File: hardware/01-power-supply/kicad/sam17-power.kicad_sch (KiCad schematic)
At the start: 31 parts, among them J1 12VAC CT 2A, J2 BUS +12/G/G/-12, J3 AC 230V IN, J4 TR1 pri (ext), U1 LM7812, U2 LM7912, U3 LM7805

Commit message: Add protective earth to module 1 and make the BOM verifiable
Closes the two documented gaps in the power-supply module, plus several
defects found while closing them.

Protective earth (design-notes.md section 13). J3 becomes a 3-position
block (L/N/PE); pin 3 drives an Earth_Protective symbol and stops there.
J5 is a new faston that carries circuit 0 V to the same chassis stud. PE
and GND stay separate nets on purpose - they meet in metal, off the
board, so fault current never runs through PCB copper.

The bond is hard rather than a ground-lift network because the panels are
galvanized sheet and the ~40 metal-bushing jacks already tie chassis to
GND at 40 points; a lift network would be shorted 40 times over. That
premise is stated explicitly, since isolated jacks would invalidate it.

J1 is a 3-position block, not 2: the transformer secondary is
centre-tapped and carries three conductors. The schematic was right and
bom.csv was stale.

Defects found while doing the above:

- J3/J4 were wired 0.36 mm off their real pins and only passed ERC
  because KiCad snaps within ~1 mm. The docstring note that "explained"
  those odd offsets was wrong; Conn_01x0N_Pin geometry is on-grid.
  build_schematic.py now aborts unless every pin has an exact wire
  vertex. This also removes the 3 off-grid warnings we had been carrying:
  ERC is now 0 errors, 0 warnings.
- The neutral ran straight through RV1's body. The varistor is 7.62 mm
  tall and J3's pins sit 2.54 apart, so it never fit; neutral now runs on
  its own lane.
- R3 is 680R, not the 2.2k the BOM listed for all three LEDs - at 5 V,
  2.2k gives ~1.3 mA and that indicator is invisible.
- bom.csv could not be cross-checked at all: it called RV1/NT1 MOV1/NTC1,
  and its C3/C4/C5 were different parts from the schematic's. It now
  carries a refs column, and check_bom.py verifies both directions.

Known gap, deliberately not fixed: the +5 V rail never leaves the board.
J2 is drawn with 4 pins (+12/GND/GND/-12) and the netlist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
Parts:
- removed J3: AC 230V IN, symbol Connector:Conn_01x02_Pin
- added J3: AC 230V IN, symbol Connector:Conn_01x03_Pin
- added J5: CHASIS, symbol Connector:Conn_01x01_Pin
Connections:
- net GND: now also J5.1 (Pin_1)
- net SEC_A: now reaches BR1.3, J1.1 (Pin_1)
- net SEC_B: now reaches BR1.4, J1.3 (Pin_3)
- net L: now reaches F1.1
- net L: now also J3.1 (Pin_1)
- net L_TR: now reaches J4.2 (Pin_2)
- net L_TR: now also NT1.2; no longer RV1.2
- net L_F: now reaches F1.2, NT1.1, RV1.1
- net N: now reaches J4.1 (Pin_1)
- net N: now also RV1.2, J3.2 (Pin_2); no longer NT1.2
- new net PE: J3.3 (Pin_3)
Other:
- note added: "J5 = puente unico GND -> chasis. PE (J3.3) sube al MISMO esparrago."
- note added: "No hay pista de PE en la PCB: la corriente de falla no pasa por la"
- note added: "placa. Apriete y ensayo de continuidad en design-notes.md sec. 13."

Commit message: Route +5V off the board via a dedicated J6 feed (closes the bus interface)
Resuelve issue #8 con la opcion C: J2 queda intacto como bus analogico
(+12/GND/GND/-12, igual para los modulos 2-7) y el +5V sale por J6, un
conector de 2 posiciones fisicamente distinto, solo hacia el modulo 2
(AD5686R + LCD, ~150 mA).

Por que C y no el header 2x5 del BOM viejo (design-notes.md 10.4):

- 10.1 ya exigia retorno del +5V dedicado hasta el punto de estrella,
  porque el backlight va conmutado por PWM: ~100 mA de flancos sobre un
  retorno compartido son mV de rebote en la referencia del DAC (a 1 V/oct,
  1 mV ~ 1.2 cents en el CV). Con conector propio la separacion es el
  conector, no una convencion de layout sobre pines GND compartidos.
- Ningun modulo recibe un +5V vivo que no usa, y el feed no se puede
  cruzar con el bus de +-12 (2 posiciones vs 4, con llave).
- La tesis no tenia bus formal que respetar (daisy-chain con jumpers,
  reportado como problema en la propia tesis); el 2x5 era del BOM viejo.

Cambios:

- build_schematic.py: J6 (Conn_01x02_Pin, girado 180 como J2) en el hueco
  sobre el riel +5V, bajada al riel sin ningun cruce de cables, retorno a
  su propio GND, nota de layout en la hoja (ASCII), comment 4 del cajetin
  y rev E -> F. De paso, el Value de #G14 sale de encima del cable de +12V
  que lo atravesaba desde la rev E y parecia etiquetar el cable equivocado.
- Netlist verificado: +5V: C10/1, C11/1, D5/2, J6/1, R3/1, U3/3; PE sigue
  aislado en J3/3. ERC 0 errores / 0 avisos; 90/90 cables con extremo
  exacto en pin; check_bom.py OK (33 en hoja / 40 designadores).
- bom.csv: J2 pasa a KK-254 4 pos comprable (ya sin la marca de no
  comprar) y entra J6 (KK-254 2 pos).
- design-notes.md: nueva seccion 10.4 con la decision y sus motivos; 7
  apunta a ella. README del modulo: checklist cerrado y seccion
  "Pendiente" reescrita como "Resuelto".

Co-Authored-By: Claude Fable 5 <noreply@anthropic.com>
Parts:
- added J6: +5V/RTN, symbol Connector:Conn_01x02_Pin
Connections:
- net +5V: now also J6.1 (Pin_1)
- net GND: now also J6.2 (Pin_2)
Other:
- note added: "J6 = feed de +5V al modulo 2 (DAC + LCD, ~150 mA), issue #8 opcion C:"
- note added: "conector aparte del bus a proposito. Rutear el retorno (J6.2) DEDICADO"
- note added: "hasta el punto de estrella, separado del retorno analogico hasta el"
- note added: "ultimo cm (design-notes.md sec. 10.1) - el backlight va conmutado."

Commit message: Assign footprints to module 1 and pin down the PCB ground rules
Fase 1 de la placa: sin huella no hay placa que crear. Los 33 componentes
quedan mapeados y verificados contra disco en cada build.

Tres huellas no las trae KiCad 10 y van en kicad/sam17.pretty:

- RV_Disc_D21mm_W5.5mm_P10.0mm: Varistor.pretty llega a D12 y el S20K275
  es un disco de 20 mm.
- NTC_Disc_D11.5mm_W4.5mm_P7.5mm: no hay libreria de termistores THT.
- Faston_6.3x0.8mm_PCB_2Leg_P5.0mm: no hay ningun faston de PCB. Lleva las
  dos patillas como el MISMO pad 1 — el simbolo de J5 tiene un pin, pero
  eso conduce corriente de falla (sec.13) y necesita las dos por resistencia
  mecanica y seccion de cobre. Es el truco que ya usa el portafusible de
  KiCad.

Decisiones que fija esta tanda (design-notes.md sec.14):

- Dos placas, no una. La fuente no espera a que se decida el formato del
  cajon, y la red de 230 V no viaja por una placa que cruza el mueble.
- Aislamiento reforzado con ranura fresada en la barrera de red. Sale casi
  gratis porque TR1 es externo: primario y secundario son dos islas y no
  hay ningun componente que cruce la barrera.
- Portafusible CERRADO (Schurter FPG4, IEC 60335-1 250VAC/10A VDE) en vez
  de clips abiertos. Ademas mide 12.5 mm contra los 24 de un clip.

Dos cosas que salieron al asignar las huellas:

- BR1 sin resolver, y es puerta antes de fabricar (sec.14.4). El nombre del
  simbolo codifica el ORDEN FISICO de patillas — KiCad trae cinco variantes
  por eso — y el esquematico eligio +-AA sin atarlo a una pieza. Las fuentes
  secundarias se contradicen sobre el DF06M/KBP206, asi que NO se afirma
  cual es: hay que leerlo del datasheet de la pieza comprada. Va tambien al
  checklist de bring-up. No bloquea el ruteo: la geometria DIP-4 es la misma
  en los cuatro casos, solo cambia que pad cae en que red.
- C1/C2 pedian footprint Radial-D10 para 4700uF/25V. No existe: un D10 a esa
  tension ronda los 470uF. El real es D16/P7.5 y ocupa el cuadruple de area,
  asi que 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
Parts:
- removed BR1: KBP206, symbol Device:D_Bridge_+-AA
- removed C1, C2: 4700uF/25V, symbol Device:C_Polarized
- removed C10, C5, C6: 100uF, symbol Device:C_Polarized
- removed C11, C7, C8: 0.1uF, symbol Device:C
- removed C3, C4, C9: 0.33uF, symbol Device:C
- removed D1, D2, D5: 1N4001, symbol Diode:1N4001
- removed D3: RED, symbol Device:LED
- removed D4: YEL, symbol Device:LED
- removed D6: GRN, symbol Device:LED
- removed F1: 250mA T, symbol Device:Fuse
- removed J1: 12VAC CT 2A, symbol Connector:Conn_01x03_Pin
- removed J2: BUS +12/G/G/-12, symbol Connector:Conn_01x04_Pin
- removed J3: AC 230V IN, symbol Connector:Conn_01x03_Pin
- removed J4: TR1 pri (ext), symbol Connector:Conn_01x02_Pin
- removed J5: CHASIS, symbol Connector:Conn_01x01_Pin
- removed J6: +5V/RTN, symbol Connector:Conn_01x02_Pin
- removed NT1: NTC 5R/2A, symbol Device:Thermistor_NTC
- removed R1, R2: 2k2, symbol Device:R
- removed R3: 680, symbol Device:R
- removed RV1: S20K275, symbol Device:Varistor
- removed U1: LM7812, symbol Regulator_Linear:LM7812_TO220
- removed U2: LM7912, symbol Regulator_Linear:LM7912_TO220
- removed U3: LM7805, symbol Regulator_Linear:LM7805_TO220
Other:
- note removed: "J5 = puente unico GND -> chasis. PE (J3.3) sube al MISMO esparrago."
- note removed: "J6 = feed de +5V al modulo 2 (DAC + LCD, ~150 mA), issue #8 opcion C:"
- note removed: "No hay pista de PE en la PCB: la corriente de falla no pasa por la"
- note removed: "conector aparte del bus a proposito. Rutear el retorno (J6.2) DEDICADO"
- note removed: "hasta el punto de estrella, separado del retorno analogico hasta el"
- note removed: "placa. Apriete y ensayo de continuidad en design-notes.md sec. 13."
- note removed: "ultimo cm (design-notes.md sec. 10.1) - el backlight va conmutado."

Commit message: Validate footprints before truncating the schematic
El commit anterior se llevo un sam17-power.kicad_sch VACIO (711 bytes, cero
componentes) sin que nada avisara.

Causa: create_schematic trunca el fichero nada mas empezar, y mis dos asserts
de huellas corrian despues. Al probar la comprobacion rompiendo un nombre a
proposito, el run aborto con la hoja ya truncada y ese fue el fichero que
entro en el commit. Una hoja vacia ademas pasa el ERC con 0 avisos, asi que
tampoco chilla por ahi.

Arreglo: las dos comprobaciones son Python puro y no necesitan servidor, asi
que se van a check_footprints(), que corre ANTES de tocar el fichero. Probado:
con un nombre de huella roto el script sale con codigo 1 y el .kicad_sch se
queda en sus 181785 bytes, intacto.

Co-Authored-By: Claude Opus 5 (1M context) <noreply@anthropic.com>
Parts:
- added BR1: KBP206, Diode_THT:Diode_Bridge_DIP-4_W7.62mm_P5.08mm, symbol Device:D_Bridge_+-AA
- added C1, C2: 4700uF/25V, Capacitor_THT:CP_Radial_D16.0mm_P7.50mm, symbol Device:C_Polarized
- added C10, C5, C6: 100uF, Capacitor_THT:CP_Radial_D6.3mm_P2.50mm, symbol Device:C_Polarized
- added C11, C7, C8: 0.1uF, Capacitor_THT:C_Disc_D5.0mm_W2.5mm_P5.00mm, symbol Device:C
- added C3, C4, C9: 0.33uF, Capacitor_THT:C_Disc_D5.0mm_W2.5mm_P5.00mm, symbol Device:C
- added D1, D2, D5: 1N4001, Diode_THT:D_DO-41_SOD81_P10.16mm_Horizontal, symbol Diode:1N4001
- added D3: RED, LED_THT:LED_D3.0mm, symbol Device:LED
- added D4: YEL, LED_THT:LED_D3.0mm, symbol Device:LED
- added D6: GRN, LED_THT:LED_D3.0mm, symbol Device:LED
- added F1: 250mA T, Fuse:Fuseholder_Cylinder-5x20mm_Schurter_FPG4_Vertical_Closed, symbol Device:Fuse
- added J1: 12VAC CT 2A, TerminalBlock:TerminalBlock_MaiXu_MX126-5.0-03P_1x03_P5.00mm, symbol Connector:Conn_01x03_Pin
- added J2: BUS +12/G/G/-12, Connector_Molex:Molex_KK-254_AE-6410-04A_1x04_P2.54mm_Vertical, symbol Connector:Conn_01x04_Pin
- added J3: AC 230V IN, TerminalBlock:TerminalBlock_MaiXu_MX126-5.0-03P_1x03_P5.00mm, symbol Connector:Conn_01x03_Pin
- added J4: TR1 pri (ext), TerminalBlock:TerminalBlock_MaiXu_MX126-5.0-02P_1x02_P5.00mm, symbol Connector:Conn_01x02_Pin
- added J5: CHASIS, sam17:Faston_6.3x0.8mm_PCB_2Leg_P5.0mm, symbol Connector:Conn_01x01_Pin
- added J6: +5V/RTN, Connector_Molex:Molex_KK-254_AE-6410-02A_1x02_P2.54mm_Vertical, symbol Connector:Conn_01x02_Pin
- added NT1: NTC 5R/2A, sam17:NTC_Disc_D11.5mm_W4.5mm_P7.5mm, symbol Device:Thermistor_NTC
- added R1, R2: 2k2, Resistor_THT:R_Axial_DIN0207_L6.3mm_D2.5mm_P10.16mm_Horizontal, symbol Device:R
- added R3: 680, Resistor_THT:R_Axial_DIN0207_L6.3mm_D2.5mm_P10.16mm_Horizontal, symbol Device:R
- added RV1: S20K275, sam17:RV_Disc_D21mm_W5.5mm_P10.0mm, symbol Device:Varistor
- added U1: LM7812, Package_TO_SOT_THT:TO-220-3_Vertical, symbol Regulator_Linear:LM7812_TO220
- added U2: LM7912, Package_TO_SOT_THT:TO-220-3_Vertical, symbol Regulator_Linear:LM7912_TO220
- added U3: LM7805, Package_TO_SOT_THT:TO-220-3_Vertical, symbol Regulator_Linear:LM7805_TO220
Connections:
- new net: D6.2 (A), R3.2
- new net: D3.2 (A), R1.2
- new net: D4.2 (A), R2.2
- new net +12V: C5.1, C7.1, D1.2 (A), J2.4 (Pin_4), R1.1, U1.3 (VO)
- new net +5V: C10.1, C11.1, D5.2 (A), J6.1 (Pin_1), R3.1, U3.3 (VO)
- new net -12V: C6.2, C8.2, D2.1 (K), D4.1 (K), J2.1 (Pin_1), U2.3 (VO)
- new net GND: C1.2, C10.2, C11.2, C2.1, C3.2, C4.1, C5.2, C6.1, C7.2, C8.1, C9.2, D3.1 (K), D6.1 (K), J1.2 (Pin_2), J2.2 (Pin_2), J2.3 (Pin_3), J5.1 (Pin_1), J6.2 (Pin_2), R2.1, U1.2 (GND), U2.1 (GND), U3.2 (GND)
- new net L: F1.1, J3.1 (Pin_1)
- new net L_F: F1.2, NT1.1, RV1.1
- new net L_TR: J4.2 (Pin_2), NT1.2
- new net N: J3.2 (Pin_2), J4.1 (Pin_1), RV1.2
- new net PE: J3.3 (Pin_3)
- new net SEC_A: BR1.3, J1.1 (Pin_1)
- new net SEC_B: BR1.4, J1.3 (Pin_3)
- new net VRAW+: BR1.1 (+), C1.1, C3.1, C9.1, D1.1 (K), D5.1 (K), U1.1 (VI), U3.1 (VI)
- new net VRAW-: BR1.2 (-), C2.2, C4.2, D2.2 (A), U2.2 (VI)
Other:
- note added: "J5 = puente unico GND -> chasis. PE (J3.3) sube al MISMO esparrago."
- note added: "J6 = feed de +5V al modulo 2 (DAC + LCD, ~150 mA), issue #8 opcion C:"
- note added: "No hay pista de PE en la PCB: la corriente de falla no pasa por la"
- note added: "conector aparte del bus a proposito. Rutear el retorno (J6.2) DEDICADO"
- note added: "hasta el punto de estrella, separado del retorno analogico hasta el"
- note added: "placa. Apriete y ensayo de continuidad en design-notes.md sec. 13."
- note added: "ultimo cm (design-notes.md sec. 10.1) - el backlight va conmutado."

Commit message: Respin module 1 schematic to LDO regulators at 650 mA/rail
Esquematico de 33 a 45 componentes. ERC 0/0, 109/109 cables con extremo
exacto, check_bom.py cuadra (45 en hoja / 52 designadores).

REGULADORES. U1 pasa a LM2940CT-12 y U2 a LM2990T-12, los dos sustitucion
directa: mismo pinout y mismo encapsulado. U1 ni siquiera cambia de simbolo —
el del LM2940 no existe en KiCad pero el del 7812 tiene el mismo mapeo.

Lo que si cambio fue la GEOMETRIA del simbolo del LM2990: misma numeracion de
pines que el 7912 pero dibujado distinto — los de potencia a +-10.16 del ancla
en vez de +-7.62, y el de masa DEBAJO del cuerpo en vez de encima. La
comprobacion de extremos exactos lo canto en el primer build; sin ella habria
pasado el ERC con tres pines colgando a 2.5 mm de su cable.

BULK DOBLE. C12 y C13 en paralelo con C1/C2: 9400 uF por riel. Con 4700 el
valle de VRAW+ a 207 V queda en 13.66 V contra los 13.6 que exige el LM2940,
o sea +0.06 V. Con 9400 sube a 14.12 V.

CONDENSADORES DE ESTABILIDAD, no de filtrado. C3 a 0.47 uF (valor de la Table
1 del datasheet). C4 deja de ser ceramico y pasa a 10 uF/35V de aluminio: el
LM2990 no acepta ceramico ahi. C5 queda especificado con ventana de ESR
(0.1-1 ohm) porque un ceramico o un low-ESR hacen oscilar al LM2940. C8 pasa a
DNP con su huella puesta: un ceramico en la salida del LM2990 le come margen
de fase.

CROWBAR en +12V: BT169D + BZX55C15 + 1k + 100nF. Si U1 muere en corto el bus
ve los 20.54 V de VRAW+ (simulado) y el abs max del AS3340 son 18: se lleva
los tres VCO. Quien abre el circuito es F1, el fusible de primario que ya
existe. Se uso el simbolo dedicado BT169D y no un Q_SCR_xxx generico porque el
sufijo de los genericos codifica el orden fisico de patillas, igual que en los
puentes — ahi ya nos quemamos una vez.

Y el zener va a 270 grados, no a 90: girado al reves su catodo cae del lado
del gate, o sea en DIRECTA, y dispararia el SCR a 0.7 V nada mas encender.
Verificado en el netlist: D7/1 (catodo) esta en +12V.

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
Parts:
- removed C4: 0.33uF, Capacitor_THT:C_Disc_D5.0mm_W2.5mm_P5.00mm, symbol Device:C
- removed U2: LM7912, Package_TO_SOT_THT:TO-220-3_Vertical, symbol Regulator_Linear:LM7912_TO220
- added C12, C13: 4700uF/25V, Capacitor_THT:CP_Radial_D16.0mm_P7.50mm, symbol Device:C_Polarized
- added C14: 100nF, Capacitor_THT:C_Disc_D5.0mm_W2.5mm_P5.00mm, symbol Device:C
- added C4: 10uF/35V, Capacitor_THT:CP_Radial_D5.0mm_P2.50mm, symbol Device:C_Polarized
- added D7: BZX55C15, Diode_THT:D_DO-35_SOD27_P7.62mm_Horizontal, symbol Device:D_Zener
- added Q1: BT169D, Package_TO_SOT_THT:TO-92_Inline, symbol Triac_Thyristor:BT169D
- added R4: 1k, Resistor_THT:R_Axial_DIN0207_L6.3mm_D2.5mm_P10.16mm_Horizontal, symbol Device:R
- added TP1: VRAW+, TestPoint:TestPoint_THTPad_D2.0mm_Drill1.0mm, symbol Connector:TestPoint
- added TP2: VRAW-, TestPoint:TestPoint_THTPad_D2.0mm_Drill1.0mm, symbol Connector:TestPoint
- added TP3: +12V, TestPoint:TestPoint_THTPad_D2.0mm_Drill1.0mm, symbol Connector:TestPoint
- added TP4: -12V, TestPoint:TestPoint_THTPad_D2.0mm_Drill1.0mm, symbol Connector:TestPoint
- added TP5: +5V, TestPoint:TestPoint_THTPad_D2.0mm_Drill1.0mm, symbol Connector:TestPoint
- added TP6: GND, TestPoint:TestPoint_THTPad_D2.0mm_Drill1.0mm, symbol Connector:TestPoint
- added U2: LM2990T-12, Package_TO_SOT_THT:TO-220-3_Vertical, symbol Regulator_Linear:LM2990SX-12
- C3: value 0.33uF -> 0.47uF
- C5: value 100uF -> 100uF/25V ESR
- C6: value 100uF -> 100uF/35V
- C8: value 0.1uF -> DNP
- U1: value LM7812 -> LM2940CT-12
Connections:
- net +12V: now also D7.1 (K), Q1.1 (A), TP3.1
- net +5V: now also TP5.1
- net -12V: now also TP4.1, U2.3 (OUT)
- net GND: now also C12.2, C13.1, C14.2, C4.1, Q1.3 (K), R4.2, TP6.1, U2.1 (GND)
- net VRAW+: now also C12.1, TP1.1
- net VRAW-: now also C13.2, C4.2, TP2.1, U2.2 (IN)
- new net: C14.1, D7.2 (A), Q1.2 (G), R4.1

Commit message: Route the 650 mA PCB: 226 segments, star ground, DRC clean
DRC de KiCad: 0 infracciones, 0 pads sin conectar, 0 errores de huella. Y los
verificadores propios en cero: cruces, pistas sobre pads ajenos, bucles de
masa, solapes, piezas fuera de margen y piezas sobre la ranura.

226 segmentos, 85 tramos, UNA sola via en toda la placa. La via es la del
retorno dedicado del +5 V, que sube por el canto derecho — la unica columna sin
ramas de masa — y entra a la estrella sin haber tocado ninguna otra rama.

Sigue sin haber plano de masa, y sigue siendo a proposito: un pour une todo con
todo por el camino mas corto, que es lo contrario de la estrella de sec.7. GND
es un arbol de tres ramas (una por columna) mas la de salidas, verificado con
union-find: cero bucles.

Lo que costo varias vueltas, por si sirve de patron:

- Los TP estaban en fila abajo y obligaban a los tres rieles a abanicarse desde
  reguladores separados 47 mm, cruzandose entre ellos. Movidos a la franja
  libre entre el bulk y los pasivos, CADA UNO EN SU COLUMNA: los cruces se
  evaporaron.
- Los LED estaban al principio de su fila y su anodo caia a 28 mm de la
  resistencia. Girados 180 y pegados a ella.
- Los cuatro pads de BR1 estan en dos columnas de dos, asi que de BR1.1 solo se
  puede salir hacia arriba o hacia la izquierda. VRAW+ acabo bajando por el
  canto izquierdo (x=5) y SEC_B mudandose a la cara de soldadura.
- Q1 pasa a TO-92_Inline_Wide: en linea, sus patas a 1.27 mm dejan 0.22 mm
  entre pads, por debajo del margen de la clase. Abiertas a 2.54 el problema
  desaparece y el SCR se dobla igual.

fab/README abre ahora con DOS avisos, no uno: el orden de patillas de BR1 y que
el tab de U2 esta a VRAW-, no a masa. Atornillarlo desnudo al mismo disipador
que U1 es un corto franco al encender.

Ranura verificada en el gerber: el Edge_Cuts tiene vertices en y = 0, 30, 32 y
200, o sea el contorno exterior y el de la fresa.

Co-Authored-By: Claude Opus 5 (1M context) <noreply@anthropic.com>
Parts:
- Q1: footprint Package_TO_SOT_THT:TO-92_Inline -> Package_TO_SOT_THT:TO-92_Inline_Wide

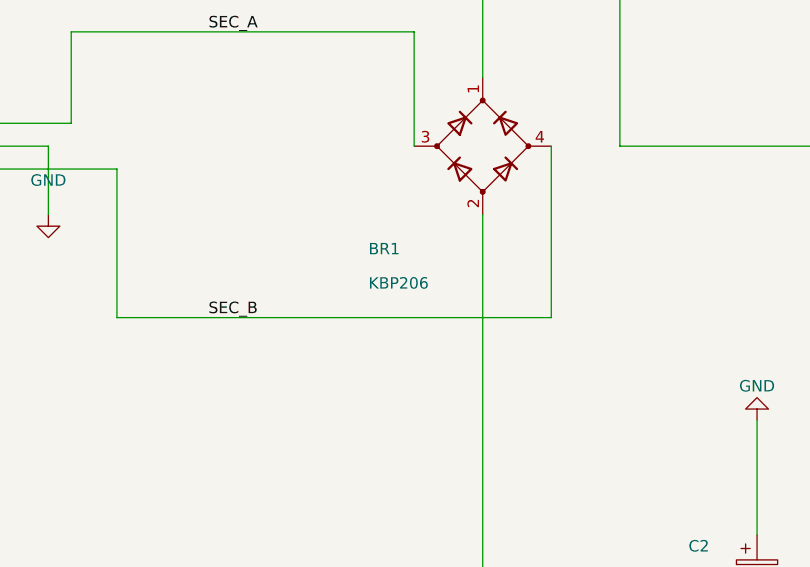
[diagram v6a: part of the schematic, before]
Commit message: Módulo 1: BR1 fijado en DB207, pinout verificado contra fuente primaria
Cierra la puerta de §14.6 (issue #11). El KBP206 del BOM no encajaba en
la huella: su case KBP es SIP de 4 patas en línea (Diodes DS21205
Rev. 12), no DIP-4. La pieza real es el DB207 (2 A/1000 V, case DB-1,
el único puente de 2 A en DIP-4 W7.62/P5.08; en RS ref. 923-5485 o TME
— Reichelt no tiene ninguno).

Pinout de dos datasheets primarios independientes que coinciden (HY
Electronic DB201-DB207 Rev. 11 y TSC HDBL101G, el que referencia la
propia huella de KiCad): fila superior − +, inferior ~ ~. Montado a 90°
cae + en pad 1, − en pad 2, ~ en pads 3/4 — exactamente lo que codifica
D_Bridge_+-AA y lo que está ruteado. Ni símbolo ni pistas cambiaron;
los gerbers quedan válidos tal cual. El riesgo restante (inserción a
180°) queda cubierto por la cruz + del silk contra la esquina + del
cuerpo, ya en el checklist de bring-up.

Co-Authored-By: Claude Fable 5 <noreply@anthropic.com>
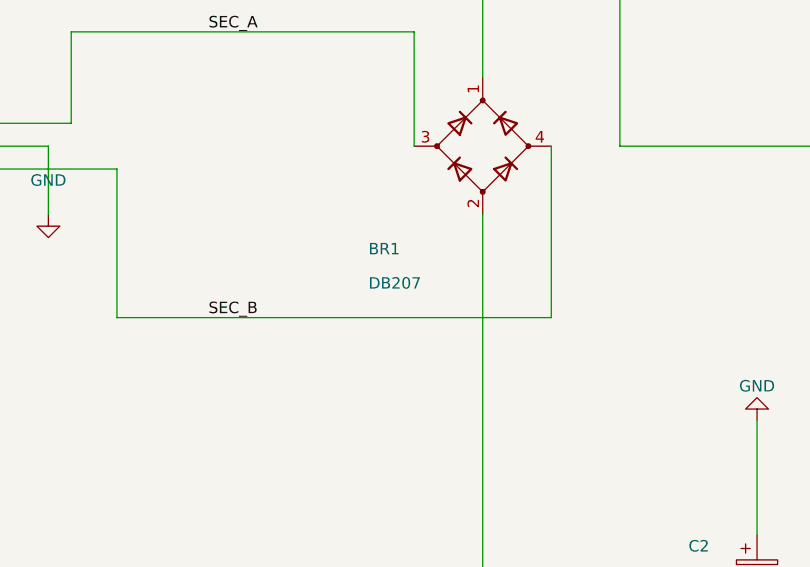
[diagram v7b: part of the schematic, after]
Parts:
- BR1: value KBP206 -> DB207
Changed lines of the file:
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@@
 			)
 		)
-		(property "Value" "KBP206"
+		(property "Value" "DB207"
 			(at 78.74 157.48000000000002 270)
 			(show_name no)
